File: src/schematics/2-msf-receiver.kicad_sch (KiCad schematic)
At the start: 80 parts, among them U2 TPS7A2036PDBVR, U203 MCP6499, U204 MCP6499, U5 TPS7A2040PDQNR

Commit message: Continued drawing up the MSF Receiver schematics.
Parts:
- removed C40, C41, C49: 4.7μF, restall-generic-capacitors:unpolarised-nominal-0402-1005, symbol restall-generic-capacitors:capacitor-unpolarised
- removed C43, C48: DNP, restall-generic-capacitors:unpolarised-nominal-0402-1005, symbol restall-generic-capacitors:capacitor-unpolarised
- removed C44, C47: 470pF, restall-generic-capacitors:unpolarised-nominal-0402-1005, symbol restall-generic-capacitors:capacitor-unpolarised
- removed C45, C46, C50: 4.7nF, restall-generic-capacitors:unpolarised-nominal-0603-1608, symbol restall-generic-capacitors:capacitor-unpolarised
- removed CONN1: header-1x4, symbol restall-generic-connectors:header-1x4
- removed CONN2: header-1x2, symbol restall-generic-connectors:header-1x2
- removed CONN3: header-1x3, symbol restall-generic-connectors:header-1x3
- removed R33, R35, R47: 390Ω, restall-generic-resistors:nominal-0402-1005, symbol restall-generic-resistors:resistor
- removed R34: 47Ω, restall-generic-resistors:nominal-0402-1005, symbol restall-generic-resistors:resistor
- removed R36, R48: 1.24kΩ, restall-generic-resistors:nominal-0402-1005, symbol restall-generic-resistors:resistor
- removed R37, R49, R52: 2.49kΩ, restall-generic-resistors:nominal-0402-1005, symbol restall-generic-resistors:resistor
- removed R38, R50: 4.99kΩ, restall-generic-resistors:nominal-0402-1005, symbol restall-generic-resistors:resistor
- removed R39, R45: 4.12kΩ, restall-generic-resistors:nominal-0402-1005, symbol restall-generic-resistors:resistor
- removed R40, R46: 64.9Ω, restall-generic-resistors:nominal-0402-1005, symbol restall-generic-resistors:resistor
- removed R41, R43: 49.9kΩ, restall-generic-resistors:nominal-0402-1005, symbol restall-generic-resistors:resistor
- removed R42, R44: 0Ω, restall-generic-resistors:nominal-0402-1005, symbol restall-generic-resistors:resistor
- removed R51: 100Ω, restall-generic-resistors:nominal-0402-1005, symbol restall-generic-resistors:resistor
- removed unit 4 of U203
- removed unit 1 of U203
- removed unit 3 of U204
- removed unit 2 of U204
- added C54, C55: 4.7μF, restall-generic-capacitors:unpolarised-nominal-0402-1005, symbol restall-generic-capacitors:capacitor-unpolarised
- added D12, D13: SD103AWS, restall-generic-sot:SOD-323, symbol restall-generic-diodes:schottky
- added R61, R62: 4.99kΩ, restall-generic-resistors:nominal-0402-1005, symbol restall-generic-resistors:resistor
- added R63, R64, R65: 33kΩ, restall-generic-resistors:nominal-0402-1005, symbol restall-generic-resistors:resistor
- added SHEET201: ~, symbol msf-owl-clock:2-msf-receiver-trf-module
- added U205: 74HC595BQ, restall-manufacturer-nexperia:DHVQFN16-2.5x3.5mm-0.5mm-expad-2x1mm, symbol restall-manufacturer-nexperia:74HC?595BQ
- renumbered U5 to U201, U2 to U202
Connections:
- net DS: now also R65.1, U205.14 (DS)
- net GND: now also C54.2, C55.2, D13.2 (A), R62.2, R63.2, R64.2, R65.2, U205.13 (~{OE}), U205.17 (GND), U205.8 (GND)
- net MSF_ANT_{-}: no longer C35.1, C36.1, C37.1, C38.1, D10.2 (A), R27.2, R29.2
- net MSF_RCV_VREF_{+2.5V}: now also D12.1 (K), R61.1
- net MSF_RCV_{+3.3V_IO}: now also C55.1, U205.10 (~{MR}), U205.16 (VCC)
- net SHCP: now also R64.1, U205.11 (SHCP)
- net STCP: now also R63.1, U205.12 (STCP)
- net 2-msf-receiver-trf/MSF_RCV_TRF: now reaches C51.2
- net at U204.12 (+): now also C54.1, D12.2 (A), R61.2, R62.1
- new net MSF_RCV_VREF_{+1.8V}: C35.1, C36.1, C37.1, C38.1, D10.2 (A), D13.1 (K), R27.2, R29.2
- new net SW_EN0: U205.15 (Q0), U205.4 (Q4)
- new net SW_EN1: U205.1 (Q1), U205.5 (Q5)
- new net SW_EN2: U205.2 (Q2), U205.6 (Q6)
- new net SW_EN3: U205.3 (Q3), U205.7 (Q7)
- no-connect marks 0 -> 1
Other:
- added sheet 2-msf-receiver-trf (2-msf-receiver-trf.kicad_sch)
- note added: "Firmware to set shift register low prior to USB SUSPEND to meet power consumption targets. The TMUX1511 is unaffected if its inputs are high whilst it is powered down, so no hardware measures are required."
- note removed: "MFB Bandpass, f_{0}≃60kHz, Q≃8, K≃-1.1 Split R2xx / R2yy provides opportunity for a Deliyannis topology if desired."
- note removed: "Programmable Amplifier, +1.5dB to +39.3dB"
- note removed: "Programmable Amplifier, +3.0dB to +45.8dB"
- note removed: "TODO: 1.25V vref (don't forget diode discharge !)"
- note removed: "TODO: 1.8V OUT"
- note removed: "TODO: ADD SWITCHES"
- note removed: "TODO: DON'T FORGET THAT THE LARGE CAPACITANCE ON THE VREF RAILS WILL NEED A DIODE TO VDD FOR DISCHARGE (OTHERWISE WILL DISCHARGE THROUGH THE OPAMPS)."
- note removed: "TODO: FOR THE SHIFT REGISTER, POWER FROM +3.3V. HOWEVER, ON USB SUSPEND, WE NEED TO ENSURE THE OUTPUTS ARE ALL ZEROES (PREFERABLY IN HARDWARE) TO AVOID BACK-POWERING THE MUXES - UNLESS THE MUXES DON'T CARE ABOUT THIS, CHECK THE DATASHEET..."
- note removed: "Tuned RF Secion 1"
- note removed: "Tuned RF Secion 2"
- moved on the sheet: C24, C25, C26, C27, C28, C29, C30, C31, C32, C33, C34, C35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

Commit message: Further elaboration of the MSF front-end.
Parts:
- added C211, C212, C213, C225, C226: 22μF, restall-generic-capacitors:unpolarised-nominal-0805-2012, symbol restall-generic-capacitors:capacitor-unpolarised
- added C214, C227, C228: DNP, restall-generic-capacitors:unpolarised-nominal-0805-2012, symbol restall-generic-capacitors:capacitor-unpolarised
- added C215, C216: 4.7μF, restall-generic-capacitors:unpolarised-nominal-0402-1005, symbol restall-generic-capacitors:capacitor-unpolarised
- renumbered C32 to C201, C52 to C202, C53 to C203, C39 to C204, C24 to C205, C25 to C206, C26 to C207, C27 to C208, C28 to C209, C29 to C210, C33 to C217, C34 to C218, C35 to C219, C36 to C220, C37 to C221, C38 to C222, C30 to C223, C31 to C224, C51 to C229, C55 to C230, C54 to C231, D9 to D201, D10 to D202, D13 to D203, D8 to D204, D11 to D205, D12 to D206, FB2 to FB201, R30 to R201, R28 to R202, R32 to R203, R29 to R204, R27 to R205, R22 to R206, R24 to R207, R23 to R208, R31 to R209, R26 to R210, R25 to R211, R59 to R212, R53 to R213, R58 to R214, R54 to R215, R55 to R216, R56 to R217, R57 to R218, R60 to R219, R61 to R220, R62 to R221, R63 to R222, R64 to R223, R65 to R224
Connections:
- net GND: now also C211.2, C212.2, C213.2, C214.2, C215.2, C216.2, C225.2, C226.2, C227.2, C228.2
- net MSF_RCV_VREF_{+2.5V}: now also C225.1, C226.1, C227.1, C228.1
- net MSF_VDD_{+3.6V}: now also U203.4 (V_{DD}), U204.4 (V_{DD}), C211.1, C212.1, C213.1, C214.1, C215.1, C216.1
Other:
- note added: "Estimated from the datasheets, the in-band PSRR@60kHz is around -96dB (the TPS7A2040 around -30dB, TPS7A2036 around -50dB, the MCP6499 around -16dB). The maximum ripple on the +5V rail when used at a maximum gain of 88.6dB is 3.6mV_{rms}, which keeps the noise at the end of the signal chain about -6dB below the signal chain's (ie. op-amp's) noise; 19.1μV_{rms} / 3.3mV_{rms} for minimum / maximum 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"
- note added: "Firmware needs to set shift register low prior to USB SUSPEND to meet power consumption targets. The TMUX1511 is unaffected if its inputs are high whilst it is powered down, so no hardware protection measures are required in the case of a firmware error."
- note removed: "Estimated from the datasheets, the in-band PSRR@60kHz is around -130dB (the TPS7A2040 around -30dB, TPS7A2036 around -50dB, the MCP6499 around -50dB). The maximum ripple on the +5V rail when used at a maximum gain of 88.6dB is 18mV_{rms}, which keeps the noise at the end of the signal chain about -6dB below the signal chain's (ie. op-amp's) noise; 19.1μV_{rms} / 3.3mV_{rms} for minimum / maximum 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"
- note removed: "Firmware to set shift register low prior to USB SUSPEND to meet power consumption targets. The TMUX1511 is unaffected if its inputs are high whilst it is powered down, so no hardware measures are required."
- note removed: "TODO: BYPASS CAPACITORS !"
- note removed: "TODO: BYPASS CAPS"
- moved on the sheet: C223, C224, D204, D205, R206, R207, R208, R209, R210, R211, U203B, U203E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

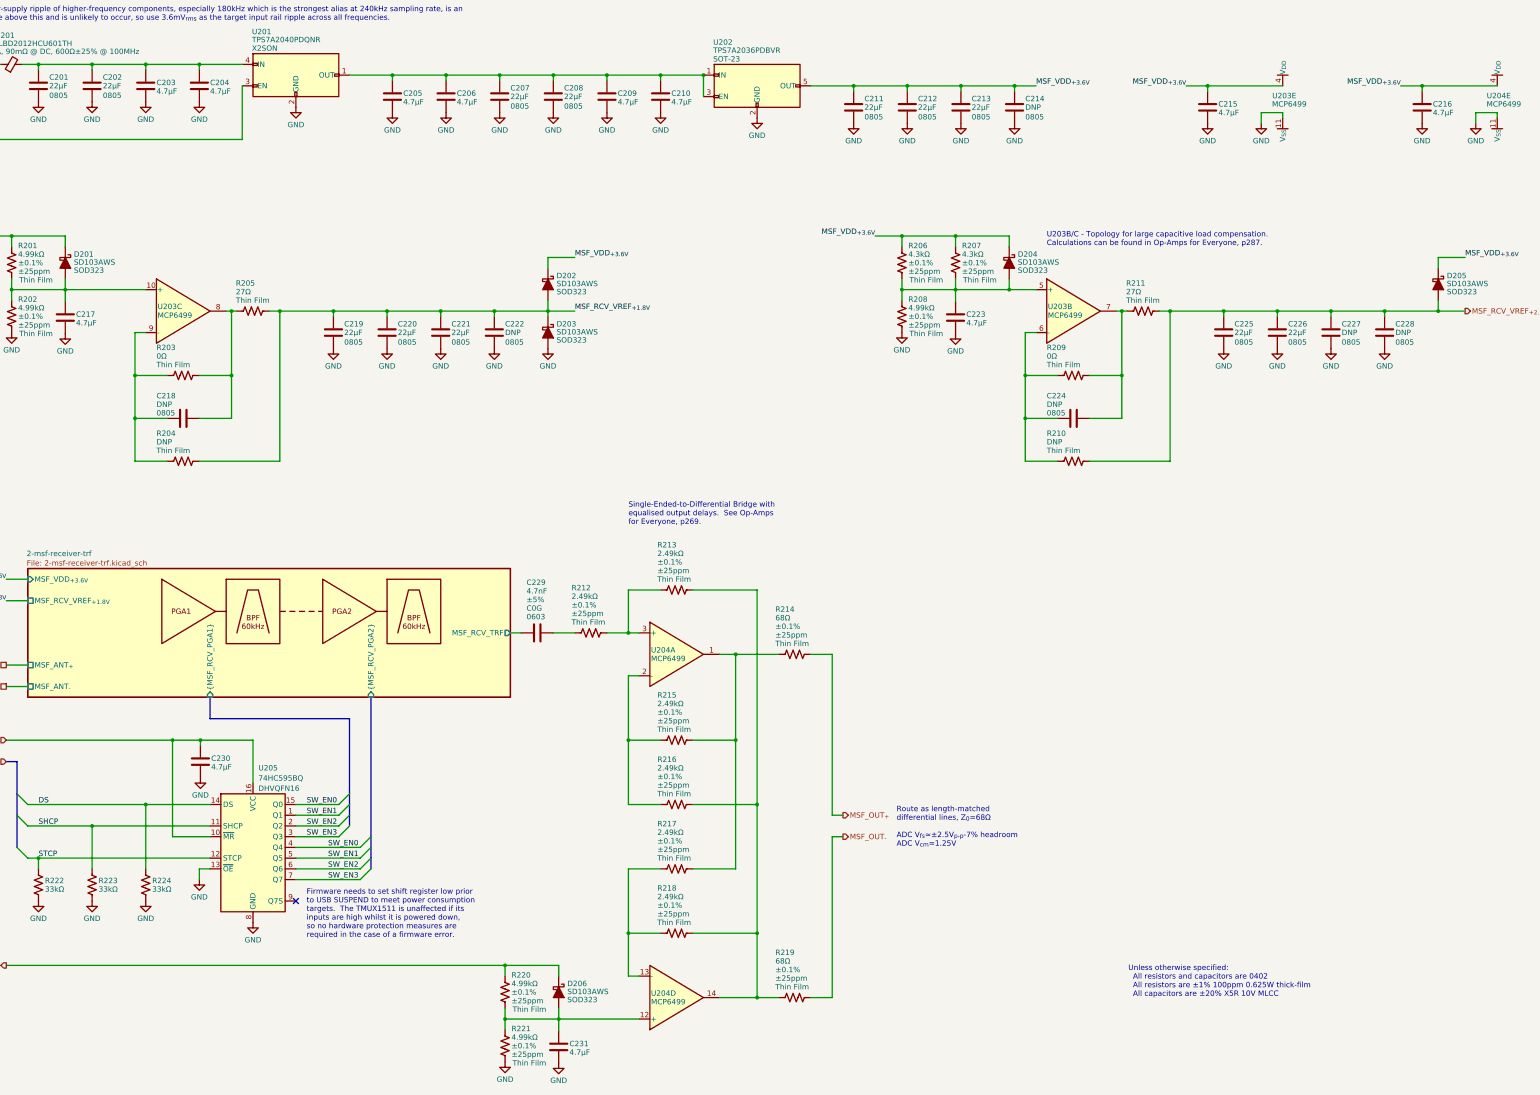
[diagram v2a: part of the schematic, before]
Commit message: Finished drawing up the audio output schematic.  The speaker selection is still to do.
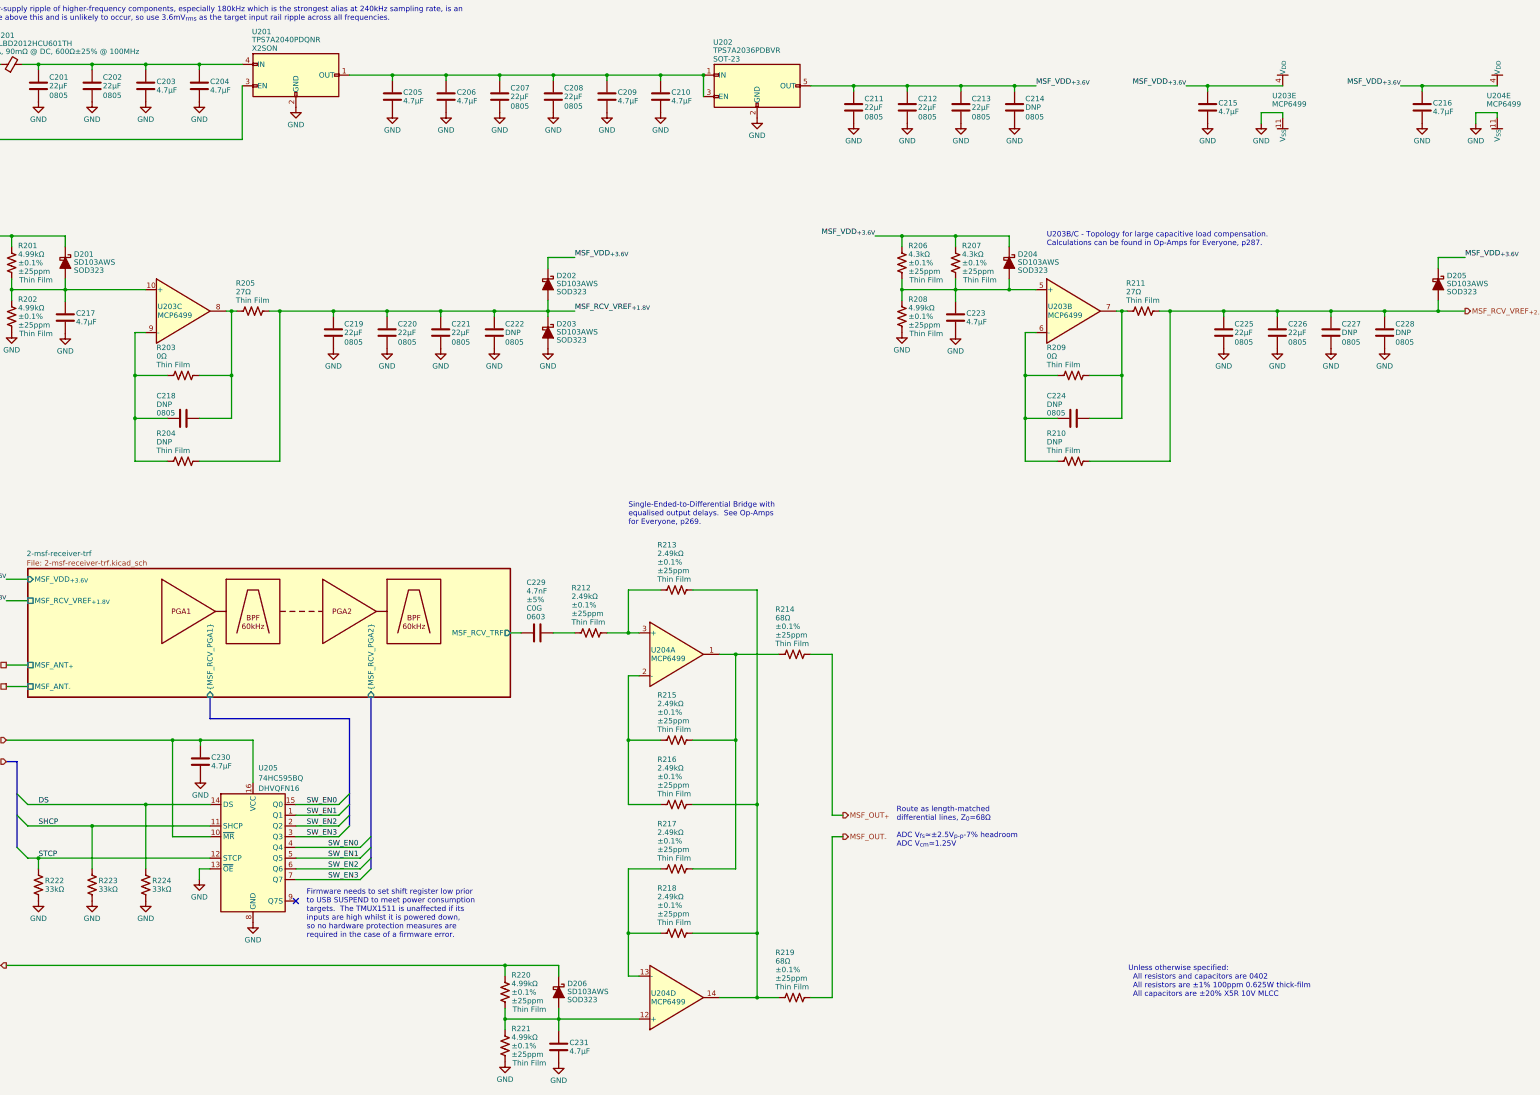
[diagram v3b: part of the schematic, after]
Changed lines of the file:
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@@
   (symbol (lib_id "restall-generic-capacitors:capacitor-unpolarised") (at 370.84 50.8 0) (unit 1)
     (in_bom yes) (on_board yes) (dnp no)
-    (property "Reference" "C216" (at 373.38 50.038 0)
+    (property "Reference" "C216" (at 373.38 49.784 0)
       (effects (font (size 1.27 1.27)) (justify left))
     )
-    (property "Value" "4.7μF" (at 373.38 52.07 0)
+    (property "Value" "4.7μF" (at 373.38 51.816 0)
       (effects (font (size 1.27 1.27)) (justify left))
     )
@@
   (symbol (lib_id "restall-generic-capacitors:capacitor-unpolarised") (at 68.58 45.72 0) (unit 1)
     (in_bom yes) (on_board yes) (dnp no)
-    (property "Reference" "C203" (at 71.12 44.958 0)
+    (property "Reference" "C203" (at 71.12 44.704 0)
       (effects (font (size 1.27 1.27)) (justify left))
     )
-    (property "Value" "4.7μF" (at 71.12 46.99 0)
+    (property "Value" "4.7μF" (at 71.12 46.736 0)
       (effects (font (size 1.27 1.27)) (justify left))
     )
@@
   (symbol (lib_id "restall-generic-capacitors:capacitor-unpolarised") (at 190.5 48.26 0) (unit 1)
     (in_bom yes) (on_board yes) (dnp no)
-    (property "Reference" "C210" (at 193.04 47.498 0)
+    (property "Reference" "C210" (at 193.04 47.244 0)
       (effects (font (size 1.27 1.27)) (justify left))
     )
-    (property "Value" "4.7μF" (at 193.04 49.53 0)
+    (property "Value" "4.7μF" (at 193.04 49.276 0)
       (effects (font (size 1.27 1.27)) (justify left))
     )
@@
   (symbol (lib_id "restall-generic-capacitors:capacitor-unpolarised") (at 81.534 205.74 0) (unit 1)
     (in_bom yes) (on_board yes) (dnp no)
-    (property "Reference" "C230" (at 84.074 204.978 0)
+    (property "Reference" "C230" (at 84.074 204.724 0)
       (effects (font (size 1.27 1.27)) (justify left))
     )
-    (property "Value" "4.7μF" (at 84.074 207.01 0)
+    (property "Value" "4.7μF" (at 84.074 206.756 0)
       (effects (font (size 1.27 1.27)) (justify left))
     )
@@
   (symbol (lib_id "restall-generic-capacitors:capacitor-unpolarised") (at 320.04 50.8 0) (unit 1)
     (in_bom yes) (on_board yes) (dnp no)
-    (property "Reference" "C215" (at 322.58 50.038 0)
+    (property "Reference" "C215" (at 322.58 49.784 0)
       (effects (font (size 1.27 1.27)) (justify left))
     )
-    (property "Value" "4.7μF" (at 322.58 52.07 0)
+    (property "Value" "4.7μF" (at 322.58 51.816 0)
       (effects (font (size 1.27 1.27)) (justify left))
     )
@@
   (symbol (lib_id "restall-generic-capacitors:capacitor-unpolarised") (at 81.28 45.72 0) (unit 1)
     (in_bom yes) (on_board yes) (dnp no)
-    (property "Reference" "C204" (at 83.82 44.958 0)
+    (property "Reference" "C204" (at 83.82 44.704 0)
       (effects (font (size 1.27 1.27)) (justify left))
     )
-    (property "Value" "4.7μF" (at 83.82 46.99 0)
+    (property "Value" "4.7μF" (at 83.82 46.736 0)
       (effects (font (size 1.27 1.27)) (justify left))
     )
@@
   (symbol (lib_id "restall-generic-capacitors:capacitor-unpolarised") (at 127 48.26 0) (unit 1)
     (in_bom yes) (on_board yes) (dnp no)
-    (property "Reference" "C205" (at 129.54 47.498 0)
+    (property "Reference" "C205" (at 129.54 47.244 0)
       (effects (font (size 1.27 1.27)) (justify left))
     )
-    (property "Value" "4.7μF" (at 129.54 49.53 0)
+    (property "Value" "4.7μF" (at 129.54 49.276 0)
       (effects (font (size 1.27 1.27)) (justify left))
     )
@@
   (symbol (lib_id "restall-generic-capacitors:capacitor-unpolarised") (at 139.7 48.26 0) (unit 1)
     (in_bom yes) (on_board yes) (dnp no)
-    (property "Reference" "C206" (at 142.24 47.498 0)
+    (property "Reference" "C206" (at 142.24 47.244 0)
       (effects (font (size 1.27 1.27)) (justify left))
     )
-    (property "Value" "4.7μF" (at 142.24 49.53 0)
+    (property "Value" "4.7μF" (at 142.24 49.276 0)
       (effects (font (size 1.27 1.27)) (justify left))
     )
@@
   (symbol (lib_id "restall-generic-capacitors:capacitor-unpolarised") (at 177.8 48.26 0) (unit 1)
     (in_bom yes) (on_board yes) (dnp no)
-    (property "Reference" "C209" (at 180.34 47.498 0)
+    (property "Reference" "C209" (at 180.34 47.244 0)
       (effects (font (size 1.27 1.27)) (justify left))
     )
-    (property "Value" "4.7μF" (at 180.34 49.53 0)
+    (property "Value" "4.7μF" (at 180.34 49.276 0)
       (effects (font (size 1.27 1.27)) (justify left))
     )
@@
   (symbol (lib_id "restall-generic-capacitors:capacitor-unpolarised") (at 49.53 100.584 0) (unit 1)
     (in_bom yes) (on_board yes) (dnp no)
-    (property "Reference" "C217" (at 52.07 99.822 0)
+    (property "Reference" "C217" (at 52.07 99.568 0)
       (effects (font (size 1.27 1.27)) (justify left))
     )
-    (property "Value" "4.7μF" (at 52.07 101.854 0)
+    (property "Value" "4.7μF" (at 52.07 101.6 0)
       (effects (font (size 1.27 1.27)) (justify left))
     )
@@
   (symbol (lib_id "restall-generic-capacitors:capacitor-unpolarised") (at 260.35 100.584 0) (unit 1)
     (in_bom yes) (on_board yes) (dnp no)
-    (property "Reference" "C223" (at 262.89 99.822 0)
+    (property "Reference" "C223" (at 262.89 99.568 0)
       (effects (font (size 1.27 1.27)) (justify left))
     )
-    (property "Value" "4.7μF" (at 262.89 101.854 0)
+    (property "Value" "4.7μF" (at 262.89 101.6 0)
       (effects (font (size 1.27 1.27)) (justify left))
     )
@@
   (symbol (lib_id "restall-generic-capacitors:capacitor-unpolarised") (at 166.37 273.304 0) (unit 1)
     (in_bom yes) (on_board yes) (dnp no)
-    (property "Reference" "C231" (at 168.91 272.542 0)
+    (property "Reference" "C231" (at 168.91 272.288 0)
       (effects (font (size 1.27 1.27)) (justify left))
     )
-    (property "Value" "4.7μF" (at 168.91 274.574 0)
+    (property "Value" "4.7μF" (at 168.91 274.32 0)
       (effects (font (size 1.27 1.27)) (justify left))
     )
